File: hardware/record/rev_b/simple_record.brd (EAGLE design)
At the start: 34.9 x 30 mm, 24 parts, among them J1 SQUALL_HEADER, J2 PJ-102AH, J3 SCREW-TERMINAL_2_0.100, J4 SCREW-TERMINAL_2_0.100, Q1 MOSFET-NCHANNELSMD

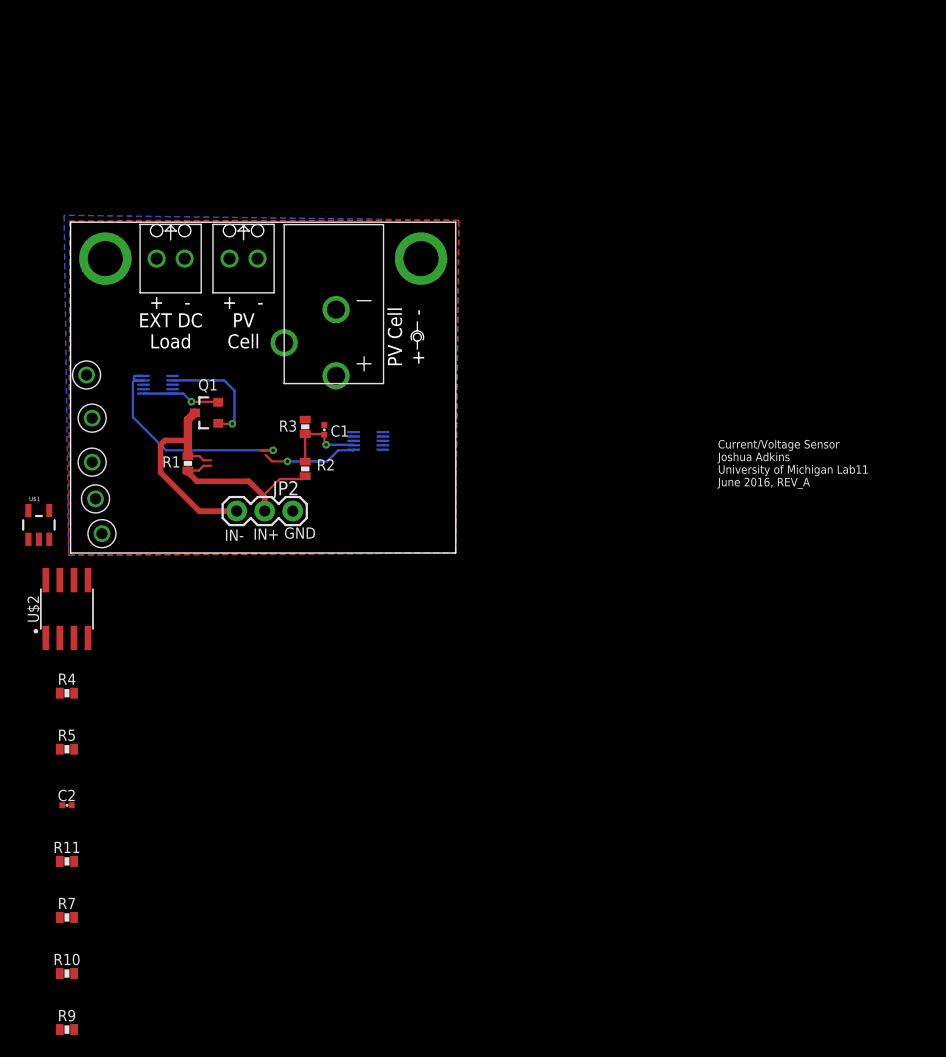
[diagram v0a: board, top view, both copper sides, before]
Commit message: updated rev_b of the board to new chip
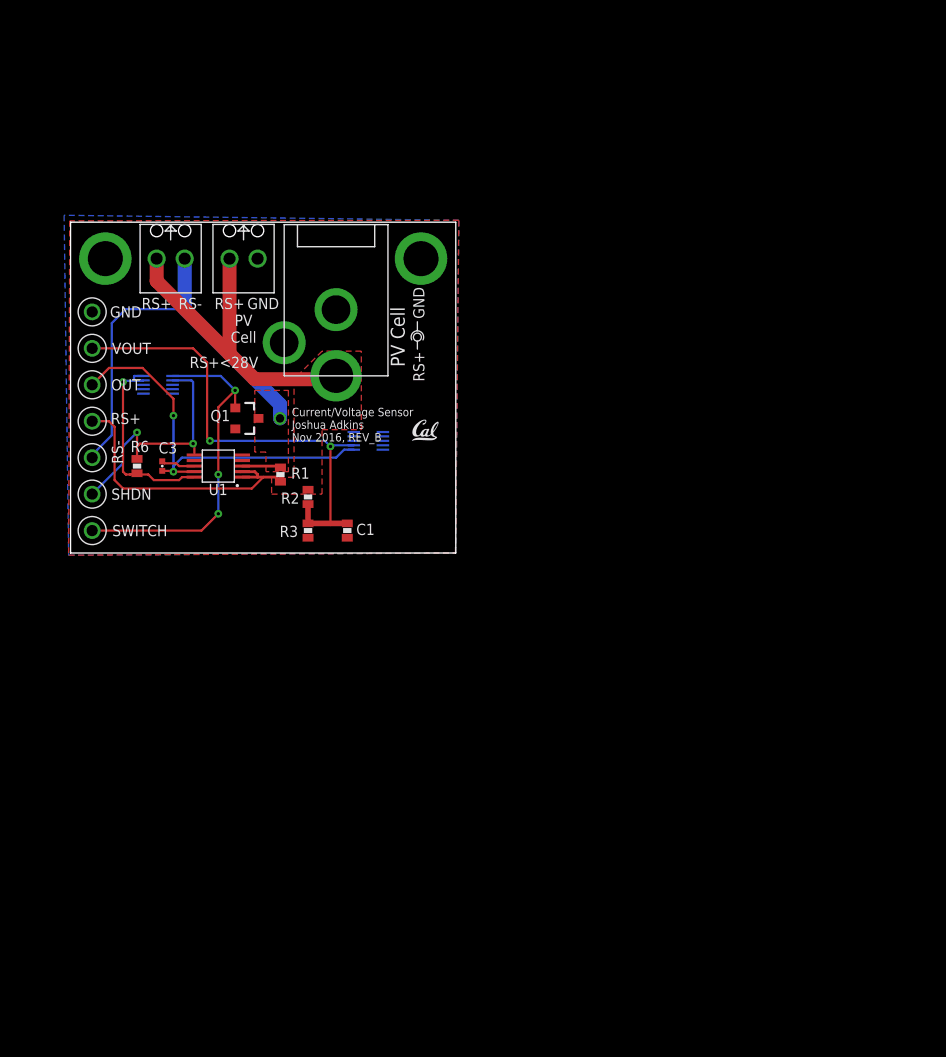
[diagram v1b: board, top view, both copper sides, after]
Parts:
- removed C2: 0.1uF, passives:0402_CAP
- removed J2: PJ-102AH, connector:PJ-102AH
- removed JP2: (no value), SparkFun-Connectors:1X03
- removed R10, R11: 10k, passives:0603-RES
- removed R4: 20.8k, passives:0603-RES
- removed R5: 9.1k, passives:0603-RES
- removed R7, R9: 190k, passives:0603-RES
- removed U$2: AD8479, chips:SOIC-8
- added C3: 1nF, passives:0402_CAP
- added R6: 100k, passives:0603-RES
- added TP1, TP7: TEST_POINT_0.040IN, headers:TESTPOINT_0.040IN
- added U$3: PJ-035C, connector:PJ-035C
- added U1: MAX9923T, chips:UMAX10
- C1: device passives:0402_CAP -> passives:0603_CAP
- U$1: value OPA344 -> UCB_CAL75MIL; device SparkFun-AnalogIC:SOT23-5 -> logos:UCB_CAL_75MIL
- moved U$1 34.6 mm to (13.5, -2.54)
- moved TP4 10.3 mm to (-15.5, 5.84)
- moved TP5 10.2 mm to (-15.5, -0.76)
- moved TP3 10.2 mm to (-15.5, -10.7)
- moved R3 9.40 mm to (4.06, -10.7), turned to 90 degrees
- moved C1 9.36 mm to (7.62, -10.7), turned to 270 degrees
- moved R1 8.44 mm to (1.56, -5.60)
- moved TP2 5.74 mm to (-15.5, 9.14)
- moved TP6 3.75 mm to (-15.5, -4.06)
- moved Q1 3.59 mm to (-1.52, -0.51), turned to 270 degrees
- moved R2 2.55 mm to (4.06, -7.62), turned to 90 degrees
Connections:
- removed net INA-: J4.1, JP2.1, Q1.3, R1.1, TP6.TESTPOINT, U$2.2
- removed net N$2: R11.1, R7.2, U$1.4
- removed net N$3: R11.2, R4.1, R5.2, U$2.1, U$2.5
- removed net N$4: R10.1, R9.1, U$1.3
- removed net N$5: R10.2, U$2.6
- removed net PGA_OUT: J1.B9, R7.1, U$1.1
- new net IN-: J4.1, Q1.3, R1.1, TP6.TESTPOINT, U1.3
- new net N$7: C3.2, U1.8
- new net OUT: C3.1, J1.B9, TP7.TESTPOINT, U1.9
- new net SHDN: J1.A4, R6.2, TP1.TESTPOINT, U1.6
- net CURRENT_SWITCH: now also J1.A2; no longer J1.A4
- net GND: now also U$3.2, U1.5, U1.7; no longer C2.2, J2.2, JP2.3, R5.1, R9.2, U$1.2, U$2.4
- net PV+: now also U$3.1, U1.1, U1.2; no longer J2.1, JP2.2, U$2.3
- net VCC: now also R6.1, U1.10; no longer C2.1, R4.2, U$1.5, U$2.7
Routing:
- net IN-: track 0.00 -> 41.8 mm, vias 0 -> 1
- net PV+: track 16.2 -> 57.9 mm
- net OUT: track 0.00 -> 36.2 mm, vias 0 -> 2
- net VOUT: track 7.78 -> 43.7 mm, vias 1 -> 2
- net SHDN: track 0.00 -> 23.4 mm, vias 0 -> 2
- net CURRENT_SWITCH: track 10.4 -> 31.7 mm, vias 1 -> 3
- net INA-: track 20.0 -> 0.00 mm
- net PGA_OUT: track 8.68 -> 0.00 mm, vias 1 -> 0
- net GND: track 7.09 -> 0.00 mm, vias 1 -> 2
- net N$7: track 0.00 -> 3.09 mm
- net VCC: track 21.4 -> 19.1 mm
- added copper zone on layer 1, net IN-
- added copper zone on layer 1, net PV+
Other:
- outline, holes or cut-outs redrawn
- board text added: "Current/Voltage Sensor Joshua Adkins Nov 2016, REV_B"
- board text added: "OUT"
- board text added: "RS+"
- board text added: "RS+<28V"
- board text added: "RS-"
- board text added: "SHDN"
- board text added: "SWITCH"
- board text added: "VOUT"
- board text removed: "+"
- board text removed: "-"
- board text removed: "Current/Voltage Sensor Joshua Adkins University of Michigan Lab11 June 2016, REV_A"
- board text removed: "EXT DC Load"
- board text removed: "IN+"
- board text removed: "IN-"

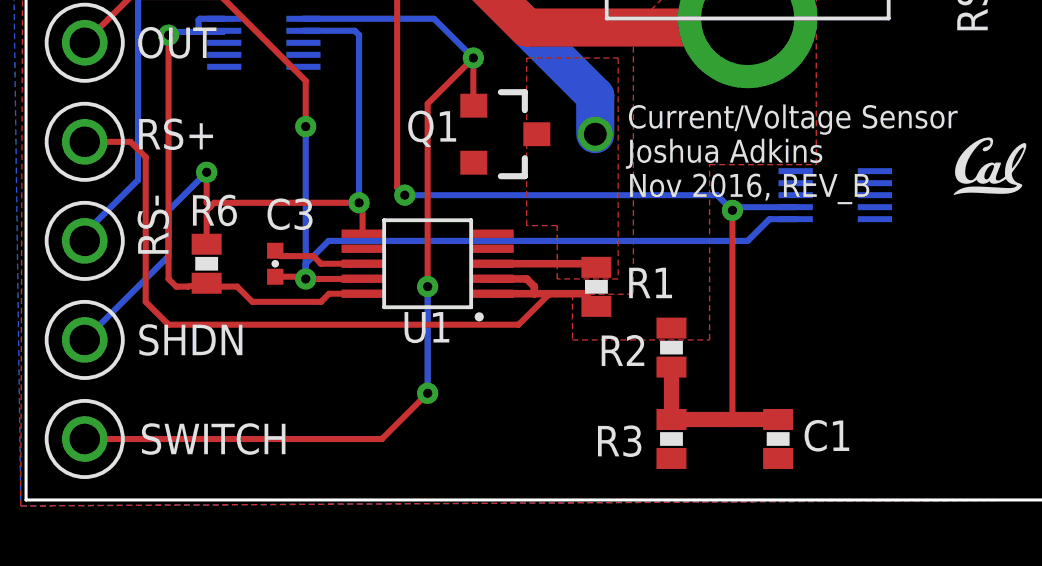
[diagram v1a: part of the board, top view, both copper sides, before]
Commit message: properly renumber parts
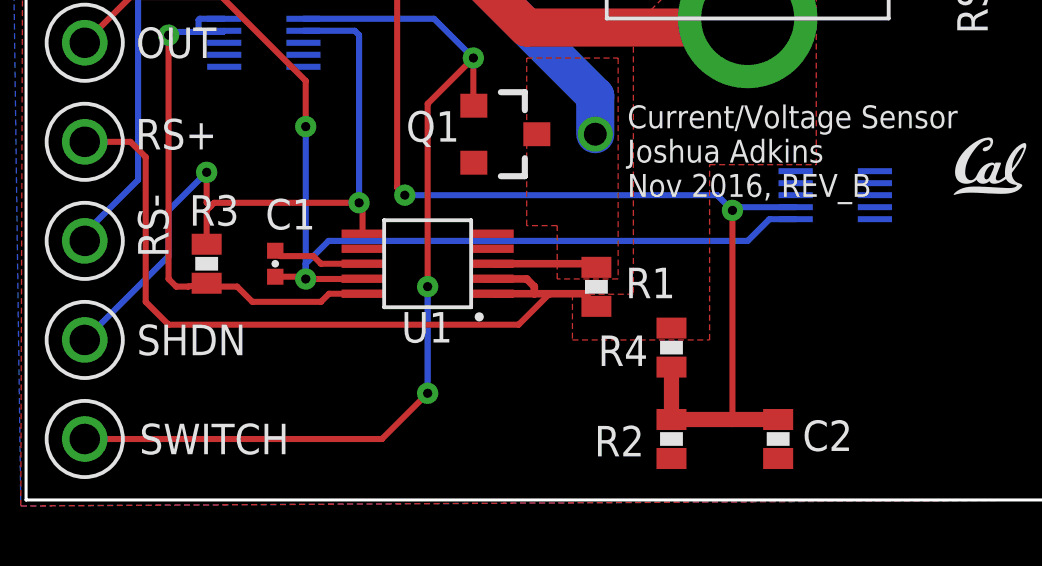
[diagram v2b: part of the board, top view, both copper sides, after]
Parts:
- removed C3: 1nF, passives:0402_CAP
- removed R6: 100k, passives:0603-RES
- removed U$3: PJ-035C, connector:PJ-035C
- added C2: 10uF, passives:0603_CAP
- added J2: SCREW-TERMINAL_2_0.100, headers:CONN_BLOCK_2
- added R4: 176k, passives:0603-RES
- C1: value 10uF -> 1nF; device passives:0603_CAP -> passives:0402_CAP
- J1: value SQUALL_HEADER -> PJ-035C; device squall:SQUALL_HEADER -> connector:PJ-035C
- J4: value SCREW-TERMINAL_2_0.100 -> SQUALL_HEADER; device headers:CONN_BLOCK_2 -> squall:SQUALL_HEADER
- R2: value 176k -> 24k
- R3: value 24k -> 100k
- moved C1 17.8 mm to (-9.14, -4.83), turned to 90 degrees
- moved R3 16.6 mm to (-11.4, -4.83)
- moved J4 16.3 mm to (0.00, 0.00), turned to 0 degrees
- moved J1 9.16 mm to (6.60, 6.35)
- moved J3 6.60 mm to (-8.38, 14.0)
- moved R2 3.05 mm to (4.06, -10.7)
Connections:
- net CURRENT_SWITCH: now also J4.A2; no longer J1.A2
- net GND: now also C2.2, J1.2, J2.1, J4.A10, J4.A9, R2.1; no longer C1.2, J1.A10, J1.A9, J3.1, R3.1, U$3.2
- net IN-: now also J3.1; no longer J4.1
- net N$7: now also C1.2; no longer C3.2
- net OUT: now also C1.1, J4.B9; no longer C3.1, J1.B9
- net PV+: now also J1.1, J2.2, R4.2; no longer J4.2, R2.2, U$3.1
- net SHDN: now also J4.A4, R3.2; no longer J1.A4, R6.2
- net VCC: now also J4.A1, J4.A3, R3.1; no longer J1.A1, J1.A3, R6.1
- net VOUT: now also C2.1, J4.B7, R2.2, R4.1; no longer C1.1, J1.B7, R2.1, R3.2
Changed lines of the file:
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@@
 <?xml version="1.0" encoding="utf-8"?>
 <!DOCTYPE eagle SYSTEM "eagle.dtd">
-<eagle version="6.6.0">
+<eagle version="6.5.0">
 <drawing>
 <settings>
@@
 <attribute name="NAME" x="-3.89" y="-0.756" size="1.016" layer="25" font="vector" ratio="12" align="bottom-center"/>
 </element>
-<element name="R2" library="passives" package="0603-RES" value="176k" x="4.064" y="-7.62" smashed="yes" rot="R90">
+<element name="R4" library="passives" package="0603-RES" value="176k" x="4.064" y="-7.62" smashed="yes" rot="R90">
 <attribute name="NAME" x="2.448" y="-7.218" size="1.016" layer="25" font="vector" ratio="12" rot="R180" align="bottom-center"/>
 </element>
-<element name="R3" library="passives" package="0603-RES" value="24k" x="4.064" y="-10.668" smashed="yes" rot="R90">
+<element name="R2" library="passives" package="0603-RES" value="24k" x="4.064" y="-10.668" smashed="yes" rot="R90">
 <attribute name="NAME" x="2.326" y="-10.232" size="1.016" layer="25" font="vector" ratio="12" rot="R180" align="bottom-center"/>
 </element>
-<element name="C1" library="passives" package="0603_CAP" value="10uF" x="7.62" y="-10.668" smashed="yes" rot="R270">
+<element name="C2" library="passives" package="0603_CAP" value="10uF" x="7.62" y="-10.668" smashed="yes" rot="R270">
 <attribute name="NAME" x="9.268" y="-11.067" size="1.016" layer="25" font="vector" ratio="12" align="bottom-center"/>
 </element>
@@
 <attribute name="NAME" x="3.364" y="-5.974" size="1.016" layer="25" font="vector" ratio="12" align="bottom-center"/>
 </element>
-<element name="J1" library="squall" package="SQUALL_HEADER" value="SQUALL_HEADER" x="0" y="0" smashed="yes">
+<element name="J4" library="squall" package="SQUALL_HEADER" value="SQUALL_HEADER" x="0" y="0" smashed="yes">
 <attribute name="DIGIKEY" value="H11617CT-ND" x="0" y="0" size="1.778" layer="27" display="off"/>
 </element>
@@
 <attribute name="DIGIKEY" value="5001K-ND" x="-15.494" y="-4.064" size="1.778" layer="27" font="vector" ratio="12" display="off"/>
 </element>
-<element name="J3" library="headers" package="CONN_BLOCK_2" value="SCREW-TERMINAL_2_0.100" x="-1.778" y="13.97" smashed="yes" rot="R180">
+<element name="J2" library="headers" package="CONN_BLOCK_2" value="SCREW-TERMINAL_2_0.100" x="-1.778" y="13.97" smashed="yes" rot="R180">
 <attribute name="MOUSER" value="651-1725656" x="-1.778" y="13.97" size="1.778" layer="27" font="vector" ratio="12" rot="R180" display="off"/>
 <attribute name="NEWARK" value="71C4107" x="-1.778" y="13.97" size="1.778" layer="27" font="vector" ratio="12" rot="R180" display="off"/>
 <attribute name="DIGIKEY" value="277-1273-ND" x="-1.778" y="13.97" size="1.778" layer="27" font="vector" ratio="12" rot="R180" display="off"/>
 </element>
-<element name="J4" library="headers" package="CONN_BLOCK_2" value="SCREW-TERMINAL_2_0.100" x="-8.382" y="13.97" smashed="yes" rot="R180">
+<element name="J3" library="headers" package="CONN_BLOCK_2" value="SCREW-TERMINAL_2_0.100" x="-8.382" y="13.97" smashed="yes" rot="R180">
 <attribute name="MOUSER" value="651-1725656" x="-8.382" y="13.97" size="1.778" layer="27" font="vector" ratio="12" rot="R180" display="off"/>
 <attribute name="NEWARK" value="71C4107" x="-8.382" y="13.97" size="1.778" layer="27" font="vector" ratio="12" rot="R180" display="off"/>
 <attribute name="DIGIKEY" value="277-1273-ND" x="-8.382" y="13.97" size="1.778" layer="27" font="vector" ratio="12" rot="R180" display="off"/>
 </element>
-<element name="U$3" library="connector" package="PJ-035C" value="PJ-035C" x="6.604" y="6.35" smashed="yes">
+<element name="J1" library="connector" package="PJ-035C" value="PJ-035C" x="6.604" y="6.35" smashed="yes">
 <attribute name="DIGIKEY" value="CP-035C-ND" x="6.604" y="6.35" size="1.778" layer="27" font="vector" ratio="12" display="off"/>
 </element>
@@
 <attribute name="DIGIKEY" value="MAX9923HEUB+-ND" x="-4.064" y="-4.826" size="1.778" layer="27" font="vector" ratio="12" rot="R90" display="off"/>
 </element>
-<element name="C3" library="passives" package="0402_CAP" value="1nF" x="-9.144" y="-4.826" smashed="yes" rot="R90">
+<element name="C1" library="passives" package="0402_CAP" value="1nF" x="-9.144" y="-4.826" smashed="yes" rot="R90">
 <attribute name="NAME" x="-8.636" y="-2.667" size="1.016" layer="25" font="vector" ratio="12" rot="R180" align="bottom-center"/>
 </element>
-<element name="R6" library="passives" package="0603-RES" value="100k" x="-11.43" y="-4.826" smashed="yes" rot="R90">
+<element name="R3" library="passives" package="0603-RES" value="100k" x="-11.43" y="-4.826" smashed="yes" rot="R90">
 <attribute name="NAME" x="-11.176" y="-2.54" size="1.016" layer="25" font="vector" ratio="12" rot="R180" align="bottom-center"/>
 </element>
@@
 <signal name="GND">
 <contactref element="Q1" pad="2"/>
-<contactref element="R3" pad="1"/>
-<contactref element="C1" pad="2"/>
-<contactref element="J1" pad="A9"/>
-<contactref element="J1" pad="A10"/>
+<contactref element="R2" pad="1"/>
+<contactref element="C2" pad="2"/>
+<contactref element="J4" pad="A9"/>
+<contactref element="J4" pad="A10"/>
 <polygon width="0.2032" layer="1" thermals="no" rank="2">
 <vertex x="-17.526" y="17.39"/>
@@
 </polygon>
 <contactref element="TP2" pad="TESTPOINT"/>
-<contactref element="J3" pad="1"/>
-<contactref element="U$3" pad="2"/>
+<contactref element="J2" pad="1"/>
+<contactref element="J1" pad="2"/>
 <contactref element="U1" pad="5"/>
 <contactref element="U1" pad="7"/>
@@
 </signal>
 <signal name="PV+">
-<contactref element="R2" pad="2"/>
+<contactref element="R4" pad="2"/>
 <contactref element="R1" pad="2"/>
 <contactref element="TP5" pad="TESTPOINT"/>
+<contactref element="J2" pad="2"/>
 <contactref element="J3" pad="2"/>
-<contactref element="J4" pad="2"/>
-<contactref element="U$3" pad="1"/>
+<contactref element="J1" pad="1"/>
 <contactref element="U1" pad="1"/>
 <contactref element="U1" pad="2"/>
@@
 <contactref element="Q1" pad="1"/>
 <contactref element="TP3" pad="TESTPOINT"/>
-<contactref element="J1" pad="A2"/>
+<contactref element="J4" pad="A2"/>
 <wire x1="-8.205" y1="3.34" x2="-3.848" y2="3.34" width="0.2032" layer="16"/>
 <wire x1="-3.848" y1="3.34" x2="-2.54" y2="2.032" width="0.2032" layer="16"/>
@@
 </signal>
 <signal name="VCC">
-<contactref element="J1" pad="A3"/>
-<contactref element="J1" pad="A1"/>
+<contactref element="J4" pad="A3"/>
+<contactref element="J4" pad="A1"/>
 <wire x1="-10.845" y1="3.34" x2="-11.66" y2="3.34" width="0.2032" layer="16"/>
 <wire x1="-11.66" y1="3.34" x2="-11.7" y2="3.3" width="0.2032" layer="16"/>
@@
 <wire x1="-10.885" y1="2.9" x2="-10.845" y2="2.94" width="0.2032" layer="16"/>
 <contactref element="U1" pad="10"/>
-<contactref element="R6" pad="1"/>
+<contactref element="R3" pad="1"/>
 <wire x1="-6.234" y1="-5.826" x2="-7.35" y2="-5.826" width="0.2032" layer="1"/>
 <wire x1="-7.35" y1="-5.826" x2="-7.62" y2="-6.096" width="0.2032" layer="1"/>
@@
 </signal>
 <signal name="VOUT">
-<contactref element="R2" pad="1"/>
-<contactref element="R3" pad="2"/>
-<contactref element="C1" pad="1"/>
-<contactref element="J1" pad="B7"/>
+<contactref element="R4" pad="1"/>
+<contactref element="R2" pad="2"/>
+<contactref element="C2" pad="1"/>
+<contactref element="J4" pad="B7"/>
 <contactref element="TP4" pad="TESTPOINT"/>
 <wire x1="4.064" y1="-8.27" x2="4.064" y2="-10.018" width="0.508" layer="1"/>
@@
 <signal name="OUT">
 <contactref element="U1" pad="9"/>
-<contactref element="C3" pad="1"/>
-<contactref element="J1" pad="B9"/>
+<contactref element="C1" pad="1"/>
+<contactref element="J4" pad="B9"/>
 <contactref element="TP7" pad="TESTPOINT"/>
 <wire x1="8.205" y1="-3.34" x2="7.328" y2="-3.34" width="0.2032" layer="16"/>
@@
 <signal name="N$7">
 <contactref element="U1" pad="8"/>
-<contactref element="C3" pad="2"/>
+<contactref element="C1" pad="2"/>
 <wire x1="-6.234" y1="-4.826" x2="-7.62" y2="-4.826" width="0.2032" layer="1"/>
 <wire x1="-7.62" y1="-4.826" x2="-7.874" y2="-4.572" width="0.2032" layer="1"/>
@@
 <signal name="SHDN">
 <contactref element="U1" pad="6"/>
-<contactref element="R6" pad="2"/>
+<contactref element="R3" pad="2"/>
 <contactref element="TP1" pad="TESTPOINT"/>
-<contactref element="J1" pad="A4"/>
+<contactref element="J4" pad="A4"/>
 <wire x1="-11.43" y1="-4.176" x2="-11.43" y2="-3.048" width="0.2032" layer="1"/>
 <wire x1="-11.43" y1="-3.048" x2="-11.303" y2="-2.921" width="0.2032" layer="1"/>
@@
 <contactref element="R1" pad="1"/>
 <contactref element="TP6" pad="TESTPOINT"/>
-<contactref element="J4" pad="1"/>
+<contactref element="J3" pad="1"/>
 <wire x1="-1.894" y1="-4.826" x2="1.442" y2="-4.826" width="0.254" layer="1"/>
 <wire x1="1.442" y1="-4.826" x2="1.562" y2="-4.946" width="0.254" layer="1"/>

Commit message: beautify
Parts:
- moved R3 4.33 mm to (-8.64, -1.52), turned to 180 degrees
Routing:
- net PV+: track 57.9 -> 53.1 mm
- net VOUT: track 43.7 -> 39.7 mm
- net IN-: track 41.8 -> 38.8 mm
- net SHDN: track 23.4 -> 20.7 mm
- net VCC: track 19.1 -> 21.4 mm
- net CURRENT_SWITCH: track 31.7 -> 29.6 mm, vias 3 -> 2
